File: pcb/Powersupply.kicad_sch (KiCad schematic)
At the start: 49 parts, among them IC3 UCC28910DR, Q3 HL2303, U3 TPS54202DDC

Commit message: fixed LEDs footprints
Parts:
- D20, D6: footprint (none) -> LED_SMD:LED_0805_2012Metric
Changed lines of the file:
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@@
 			)
 		)
-		(property "Footprint" ""
+		(property "Footprint" "LED_SMD:LED_0805_2012Metric"
 			(at 232.41 146.05 0)
 			(effects
@@
 			)
 		)
-		(property "Footprint" ""
+		(property "Footprint" "LED_SMD:LED_0805_2012Metric"
 			(at 215.9 146.05 0)
 			(effects

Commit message: fixed pcb import errors
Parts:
- D19: footprint (none) -> LED_SMD:LED_0805_2012Metric
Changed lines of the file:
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@@
 			)
 		)
-		(property "Footprint" ""
+		(property "Footprint" "LED_SMD:LED_0805_2012Metric"
 			(at 243.84 104.14 0)
 			(effects

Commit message: updated inductance footprints
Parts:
- L1: value 250u -> 150u; footprint Inductor_SMD:L_6.3x6.3_H3 -> Inductor_SMD:L_SXN_SMDRI127
- L3: footprint Inductor_SMD:L_Coilcraft_XAL7030-152 -> Inductor_SMD:L_SXN_SMDRI125
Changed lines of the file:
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@@
 		(dnp no)
 		(property "Reference" "L1"
-			(at 192.024 83.82 90)
-			(effects
-				(font
-					(size 1.27 1.27)
-				)
-			)
-		)
-		(property "Value" "250u"
-			(at 192.024 86.36 90)
-			(effects
-				(font
-					(size 1.27 1.27)
-				)
-			)
-		)
-		(property "Footprint" "Inductor_SMD:L_6.3x6.3_H3"
+			(at 192.024 83.312 90)
+			(effects
+				(font
+					(size 1.27 1.27)
+				)
+			)
+		)
+		(property "Value" "150u"
+			(at 192.024 85.852 90)
+			(effects
+				(font
+					(size 1.27 1.27)
+				)
+			)
+		)
+		(property "Footprint" "Inductor_SMD:L_SXN_SMDRI127"
 			(at 191.77 81.28 0)
 			(effects
@@
 			)
 		)
-		(property "Description" "Inductor"
-			(at 191.77 81.28 0)
-			(effects
-				(font
-					(size 1.27 1.27)
-				)
-				(hide yes)
+		(property "Description" "CYH127-150UH"
+			(at 192.278 88.138 90)
+			(effects
+				(font
+					(size 1.27 1.27)
+				)
 			)
 		)
@@
 			)
 		)
-		(property "Footprint" "Inductor_SMD:L_Coilcraft_XAL7030-152"
+		(property "Footprint" "Inductor_SMD:L_SXN_SMDRI125"
 			(at 133.35 146.05 0)
 			(effects
@@
 			)
 		)
-		(property "Description" "MDA7030-150M"
-			(at 138.176 142.494 90)
-			(effects
-				(font
+		(property "Description" "CYH127-15UH"
+			(at 137.414 142.494 90)
+			(effects
+				(font

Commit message: added DNP for fabrication and 2P molex connector, minor fixes
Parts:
- C10, C12, C14, C19: now not fitted
- TP28: footprint Connector_PinHeader_1.00mm:PinHeader_1x01_P1.00mm_Vertical -> Connector_PinHeader_2.54mm:PinHeader_1x01_P2.54mm_Vertical; now not fitted
- TP29: footprint Connector_PinHeader_1.00mm:PinHeader_1x01_P1.00mm_Vertical -> Connector_PinHeader_2.54mm:PinHeader_1x01_P2.54mm_Vertical
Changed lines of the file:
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@@
 			)
 		)
-		(property "Footprint" "Connector_PinHeader_1.00mm:PinHeader_1x01_P1.00mm_Vertical"
+		(property "Footprint" "Connector_PinHeader_2.54mm:PinHeader_1x01_P2.54mm_Vertical"
 			(at 238.76 113.03 0)
 			(effects
@@
 		(in_bom yes)
 		(on_board yes)
-		(dnp no)
+		(dnp yes)
 		(property "Reference" "C14"
 			(at 162.56 72.39 90)
@@
 		(in_bom yes)
 		(on_board yes)
-		(dnp no)
+		(dnp yes)
 		(property "Reference" "C10"
 			(at 49.784 148.844 0)
@@
 		(in_bom yes)
 		(on_board yes)
-		(dnp no)
+		(dnp yes)
 		(property "Reference" "TP28"
 			(at 241.554 72.898 0)
@@
 			)
 		)
-		(property "Footprint" "Connector_PinHeader_1.00mm:PinHeader_1x01_P1.00mm_Vertical"
+		(property "Footprint" "Connector_PinHeader_2.54mm:PinHeader_1x01_P2.54mm_Vertical"
 			(at 248.92 78.74 0)
 			(effects
@@
 		(in_bom yes)
 		(on_board yes)
-		(dnp no)
+		(dnp yes)
 		(property "Reference" "C19"
 			(at 217.17 94.234 0)
@@
 		(in_bom yes)
 		(on_board yes)
-		(dnp no)
+		(dnp yes)
 		(property "Reference" "C12"
 			(at 81.28 93.9799 0)

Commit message: removed GNDPWR
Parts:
- removed JP10: SolderJumper_3_Open, Jumper:SolderJumper-3_P1.3mm_Open_RoundedPad1.0x1.5mm, symbol Jumper:SolderJumper_3_Open
- added JP10: SolderJumper_2_Open, Jumper:SolderJumper-2_P1.3mm_Open_RoundedPad1.0x1.5mm, symbol Jumper:SolderJumper_2_Open
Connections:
- net GNDPWR is gone; now on net GND: FB1.2, JP26.1 (A)
- net GND: now also JP10.2 (B); no longer FB1.1
- net RECT-: now also JP10.1 (A)
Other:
- moved on the sheet: FB1

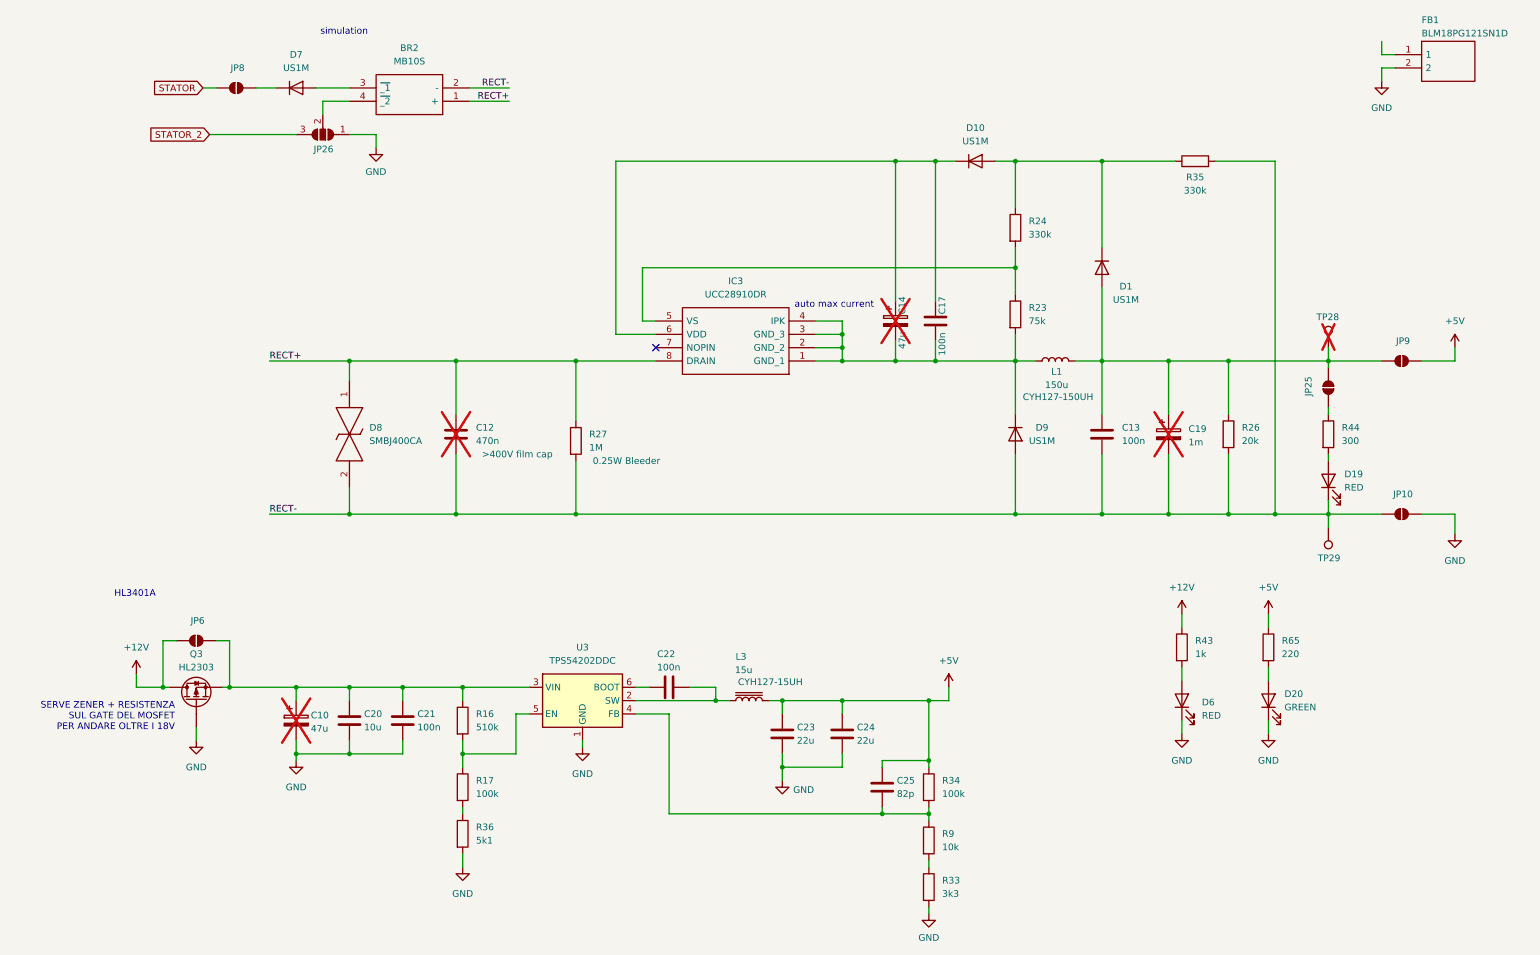
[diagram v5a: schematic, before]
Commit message: fixed 3.3 and 3V3
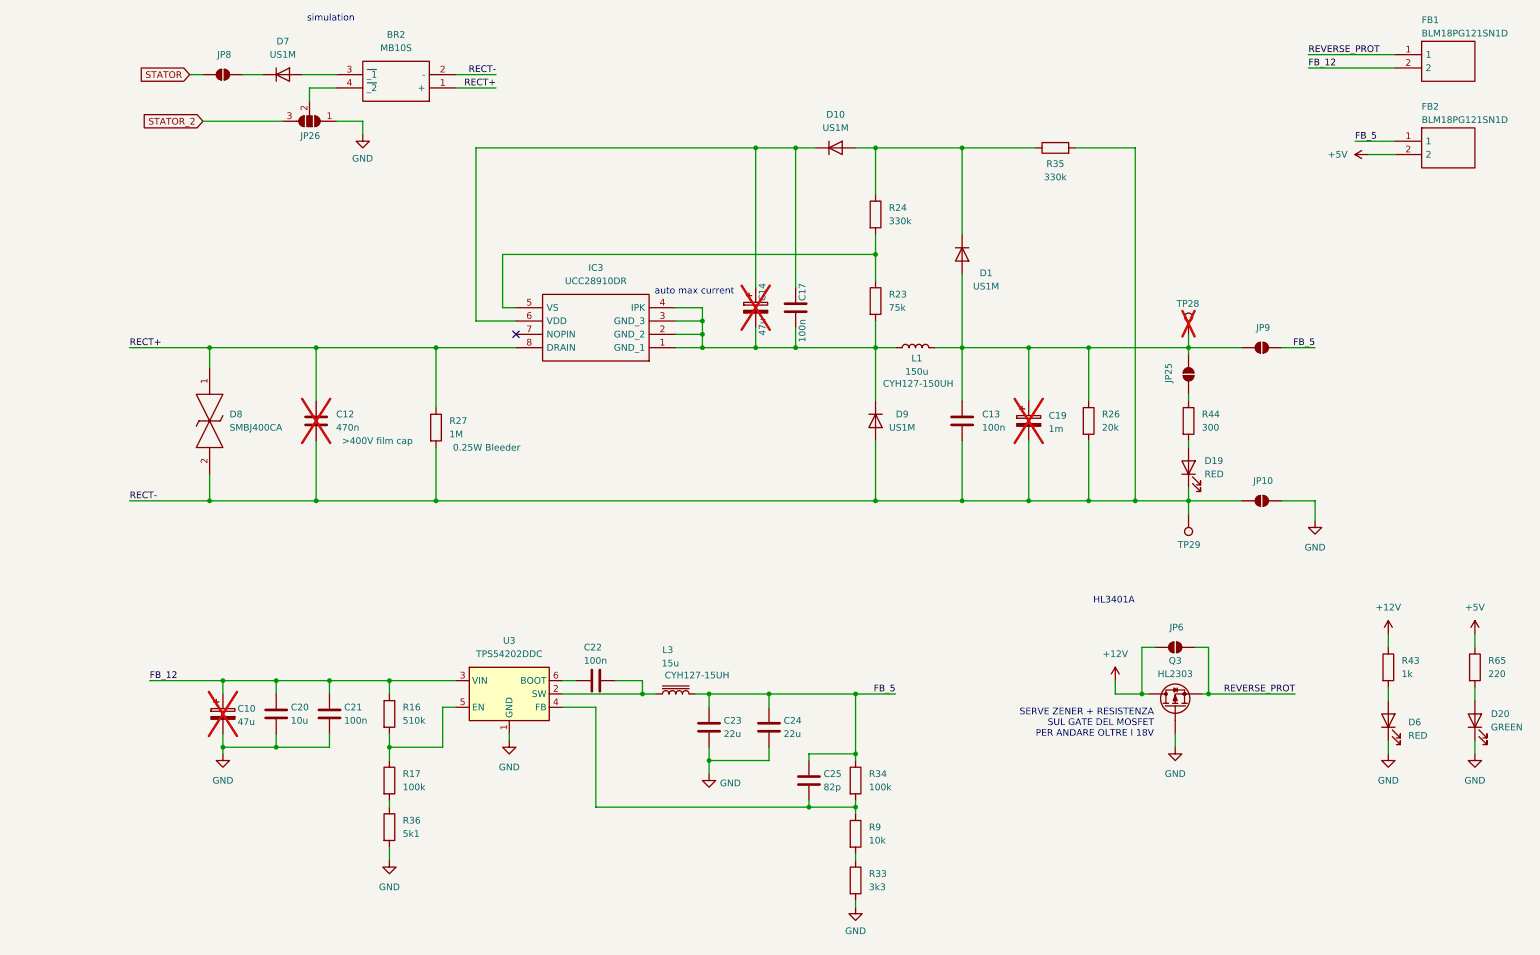
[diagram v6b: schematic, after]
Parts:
- added FB2: BLM18PG121SN1D, SamacSys_Parts:BLM18SP221SN1B, symbol SamacSys_Parts:BLM18PG121SN1D
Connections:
- net +5V: now also FB2.2; no longer C23.1, C24.1, C25.1, JP9.2 (B), L3.2, R34.1
- net GND: no longer FB1.2
- net FB_12: now reaches C10.1, C20.1, C21.1, R16.1, U3.3 (VIN)
- net FB_12: now also FB1.2; no longer JP6.2 (B), Q3.2 (S)
- net REVERSE_PROT: now reaches FB1.1
- net REVERSE_PROT: now also JP6.2 (B), Q3.2 (S)
- new net FB_5: C23.1, C24.1, C25.1, FB2.1, JP9.2 (B), L3.2, R34.1
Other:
- moved on the sheet: BR2, C10, C12, C13, C14, C17, C19, C20, C21, C22, C23, C24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

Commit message: added schottky OR-ing to DC converters
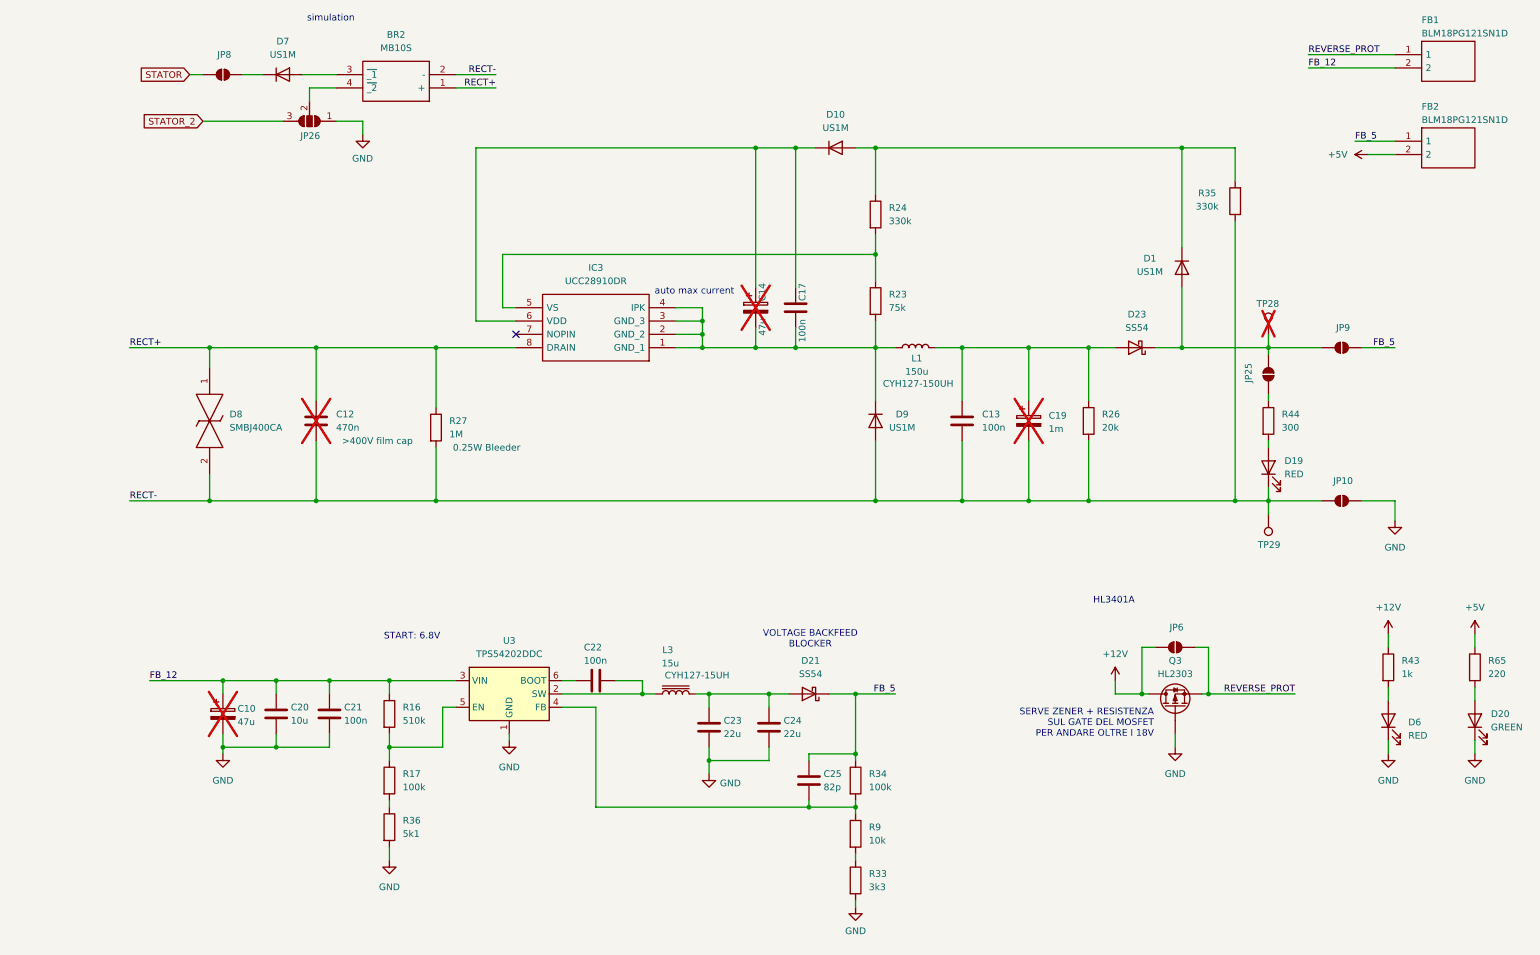
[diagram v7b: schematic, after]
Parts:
- added D21, D23: SS54, Diode_SMD:D_SMA, symbol Diode:SS34
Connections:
- net FB_5: now also D21.1 (K); no longer C23.1, C24.1, L3.2
- net RECT-: now also R35.1; no longer R35.2
- net at D1.2 (A), JP25.2 (B), JP9.1 (A)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: now also D23.1 (K); no longer C13.1, C19.1, L1.2, R26.1
- net at D1.1 (K), D10.2 (A), R24.1: now also R35.2; no longer R35.1
- new net: C13.1, C19.1, D23.2 (A), L1.2, R26.1
- new net: C23.1, C24.1, D21.2 (A), L3.2
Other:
- note added: "START: 6.8V"
- note added: "VOLTAGE BACKFEED BLOCKER"
- moved on the sheet: D1, D19, JP10, JP25, JP9, R35, R44, TP28, TP29

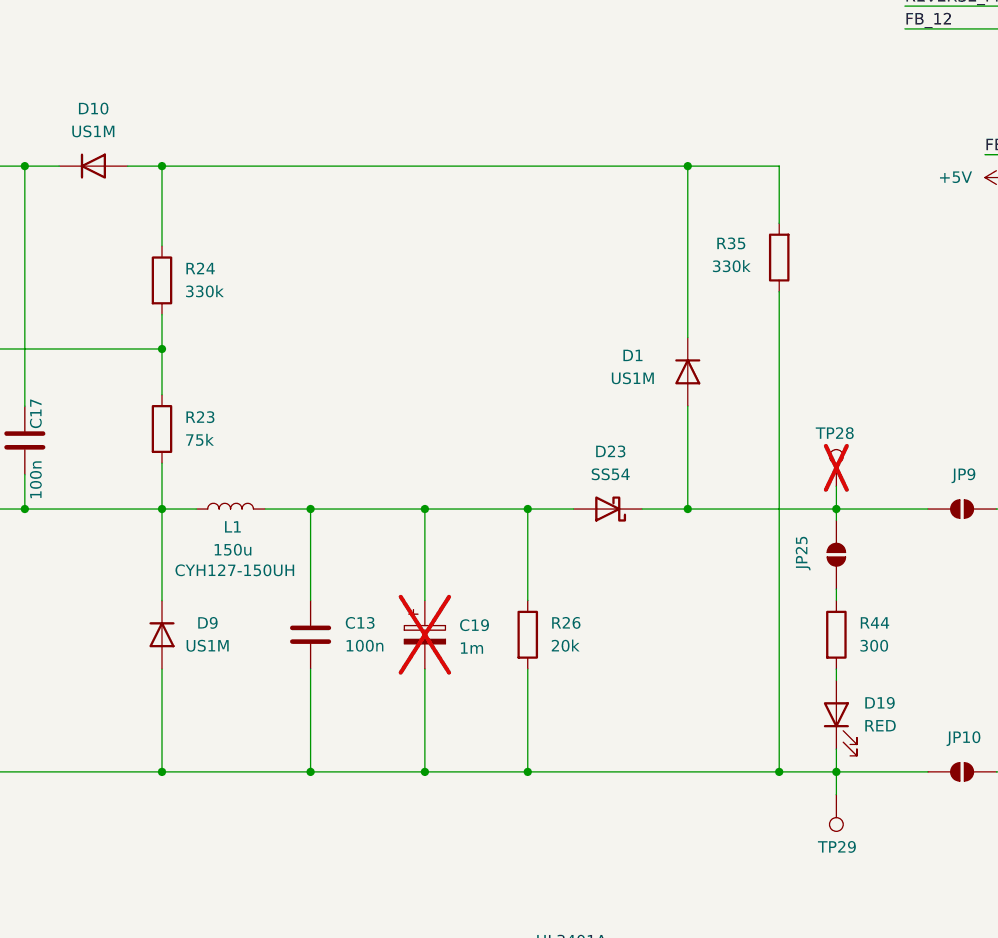
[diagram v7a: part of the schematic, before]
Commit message: moved the bulk cap outside
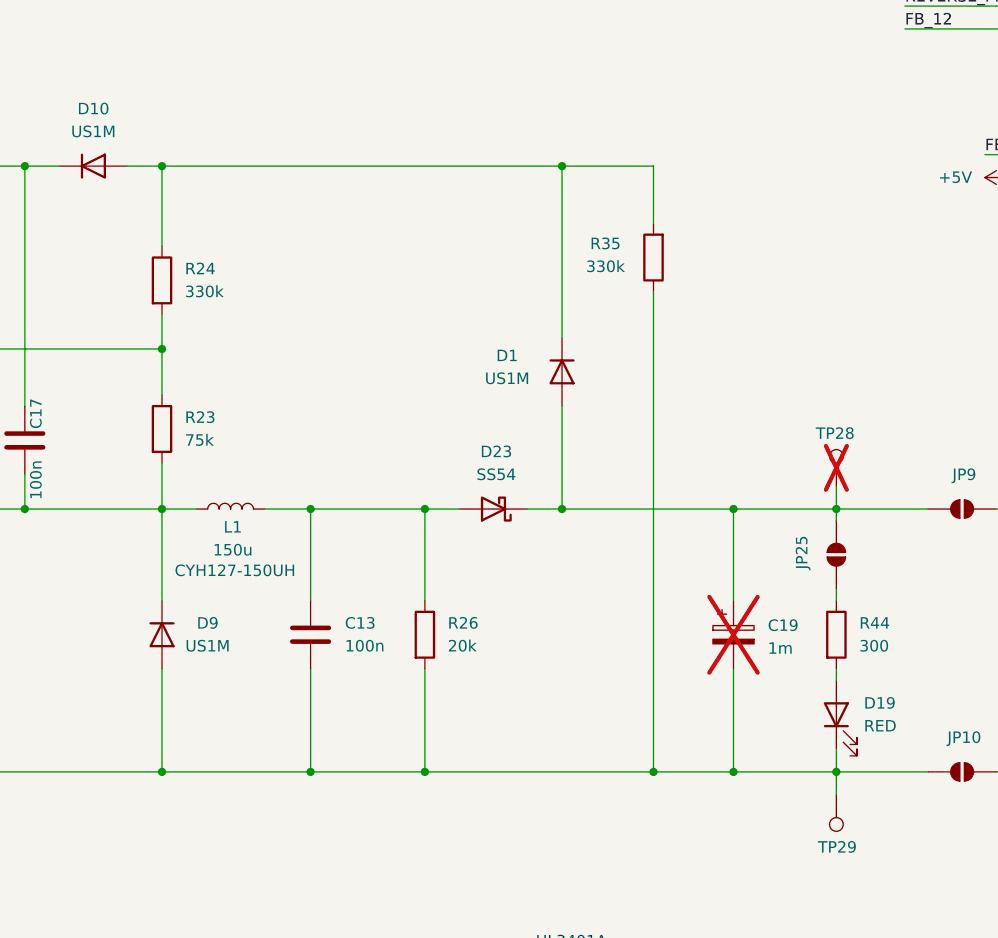
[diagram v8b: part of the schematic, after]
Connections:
- net at D1.2 (A), D23.1 (K), JP25.2 (B)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: now also C19.1
- net at C13.1, D23.2 (A), L1.2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: no longer C19.1
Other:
- moved on the sheet: C19, D1, D23, R26, R35
